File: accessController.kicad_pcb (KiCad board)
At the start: 2 copper layers, 75.6 x 81.9 mm, 36 parts, among them J1 220V AC POWER, J2 Load, J3 Screw_Terminal_01x02, J4 GPIO, J5 Conn_01x04, K1 HJR-3FF-5VDC-S-Z, Q1 BSS138, SW1 SW_Push, SW2 SW_Push, U1 ACS712xLCTR-20A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

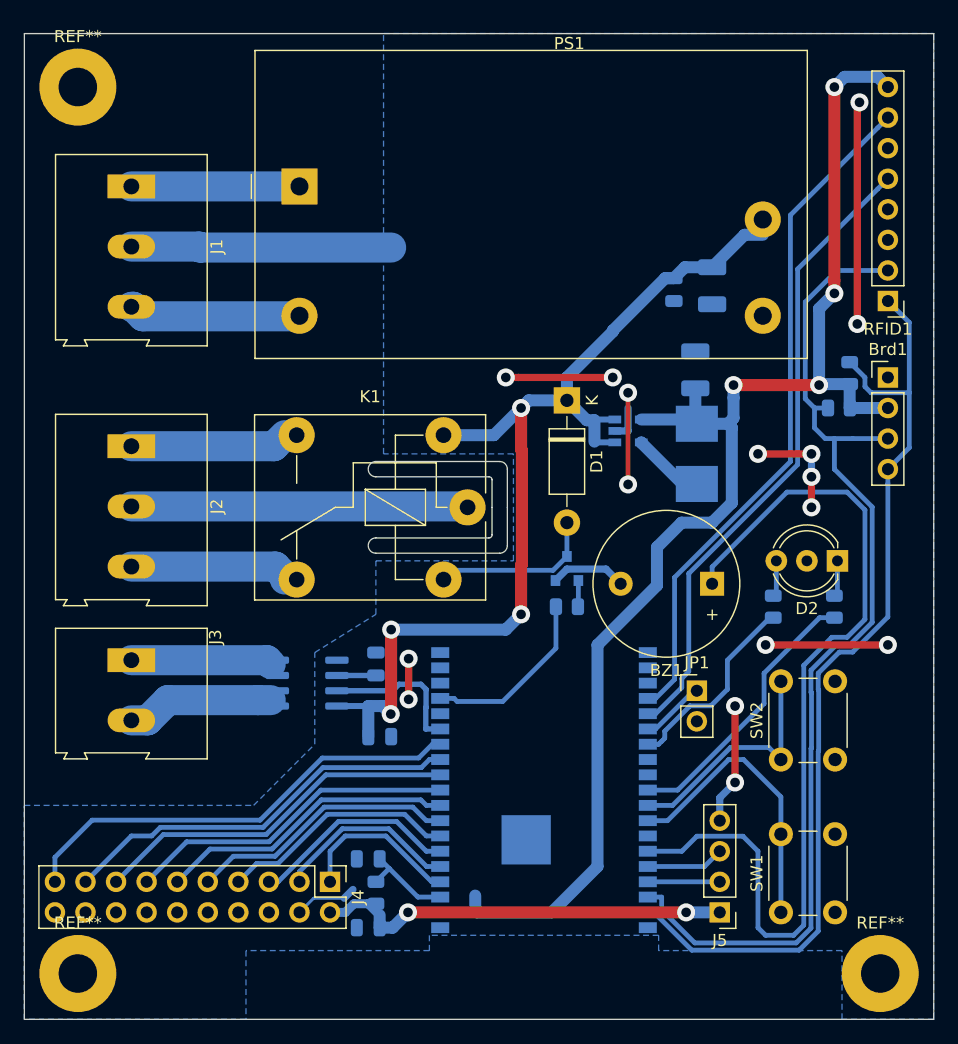
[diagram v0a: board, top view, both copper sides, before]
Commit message: Update, reduce unfilled zones for easier milling
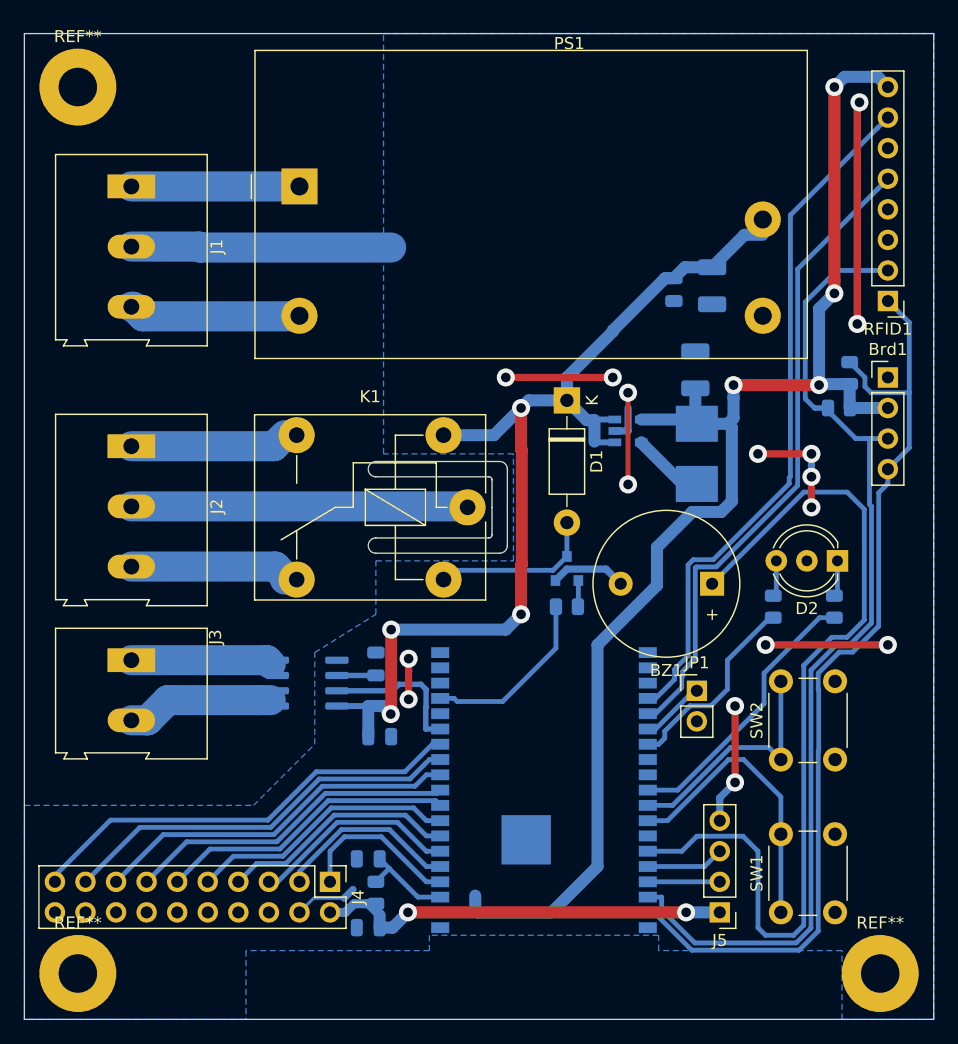
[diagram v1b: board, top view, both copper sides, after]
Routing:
- net Net-(Brd1-Pad3): track 87.3 -> 85.5 mm
- net Net-(RFID1-Pad7): track 56.9 -> 57.9 mm
- net Net-(RFID1-Pad5): track 53.1 -> 54.1 mm
- net Net-(J4-Pad19): track 37.9 -> 37.0 mm
- net Net-(BZ1-Pad1): track 75.6 -> 74.7 mm
